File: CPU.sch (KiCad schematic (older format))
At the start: 13 parts, among them J4 SWD, U1 STM32F405RGTx, Y1 8MHz

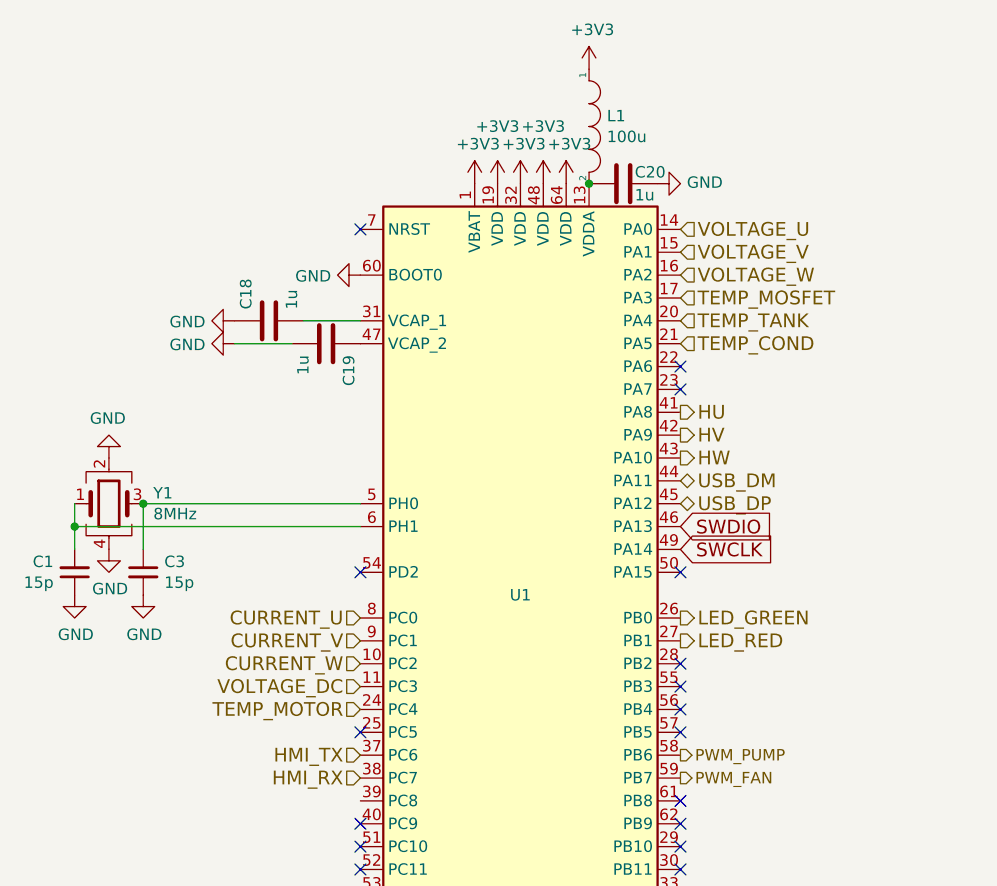
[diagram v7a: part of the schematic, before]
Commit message: - switched fan MOSFET for something beefier - switched fan diode for SMC - added BOOT0 jumper - changed fan header to 3pin - removed motor thermistor - reused condenser thermistor for return temperature sensing
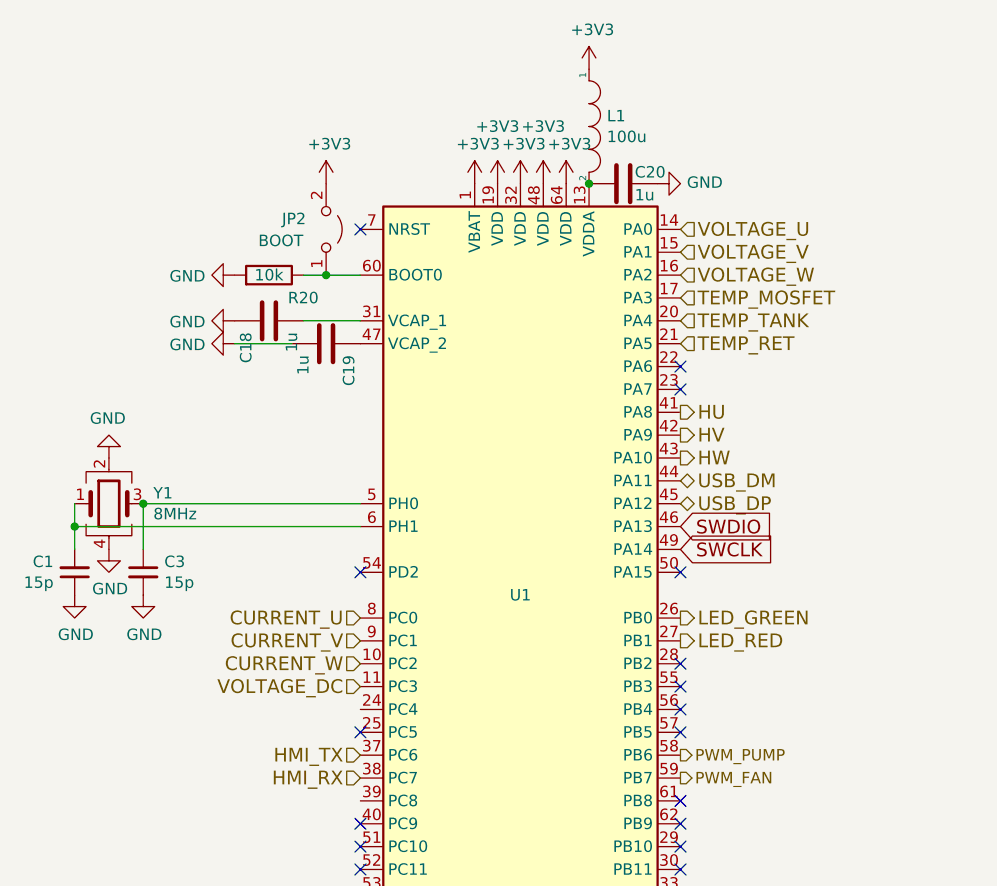
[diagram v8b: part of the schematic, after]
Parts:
- added JP2: BOOT, Jumper:SolderJumper-2_P1.3mm_Open_RoundedPad1.0x1.5mm, symbol Jumper:Jumper_2_Open
- added R20: 10k, Resistor_SMD:R_0805_2012Metric, symbol Device:R
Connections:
- net +3V3: now also JP2.2 (B)
- net GND: now also R20.2; no longer U1.60 (BOOT0)
- net TEMP_COND renamed TEMP_RET
- net TEMP_MOTOR: no longer names the net of U1.24 (PC4)
- new net: JP2.1 (A), R20.1, U1.60 (BOOT0)
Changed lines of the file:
@@
 Text HLabel 5000 4100 0    60   Input ~ 0
 HMI_RX
-Text HLabel 5000 3800 0    60   Input ~ 0
-TEMP_MOTOR
 Text HLabel 6400 4900 2    60   Output ~ 0
 LW
@@
 LU
 Text HLabel 6400 2200 2    60   Input ~ 0
-TEMP_COND
+TEMP_RET
 Text HLabel 6400 2500 2    60   Output ~ 0
 HU
@@
 $EndComp
 $Comp
-L Device:C C18
-U 1 1 53F757B5
-P 4600 2100
-AR Path="/53F757B5" Ref="C18"  Part="1"
-AR Path="/5899E230/53F757B5" Ref="C18"  Part="1"
-F 0 "C18" H 4650 2200 50  0000 L CNN
-F 1 "1u" H 4650 2000 50  0000 L CNN
-F 2 "Capacitor_SMD:C_0805_2012Metric" H 4600 2100 60  0001 C CNN
-F 3 "" H 4600 2100 60  0001 C CNN
-	1    4600 2100
-	0    -1   -1   0
-$EndComp
-$Comp
 L Device:C C19
 U 1 1 53F757AE
@@
 NoConn ~ 6400 3200
 NoConn ~ 6400 3600
-$Comp
-L power:GND #PWR0116
-U 1 1 5EE78F0F
-P 5000 1900
-F 0 "#PWR0116" H 5000 1650 50  0001 C CNN
-F 1 "GND" V 5005 1772 50  0000 R CNN
-F 2 "" H 5000 1900 50  0001 C CNN
-F 3 "" H 5000 1900 50  0001 C CNN
-	1    5000 1900
-	0    1    1    0
-$EndComp
 NoConn ~ 6400 3800
 NoConn ~ 6400 3900
@@
 NoConn ~ 6400 4400
 NoConn ~ 6400 3700
+$Comp
+L Device:C C18
+U 1 1 53F757B5
+P 4600 2100
+AR Path="/53F757B5" Ref="C18"  Part="1"
+AR Path="/5899E230/53F757B5" Ref="C18"  Part="1"
+F 0 "C18" H 4650 2200 50  0000 L CNN
+F 1 "1u" H 4650 2000 50  0000 L CNN
+F 2 "Capacitor_SMD:C_0805_2012Metric" H 4600 2100 60  0001 C CNN
+F 3 "" H 4600 2100 60  0001 C CNN
+	1    4600 2100
+	0    -1   1    0
+$EndComp
+$Comp
+L power:GND #PWR0116
+U 1 1 5EE78F0F
+P 4450 1900
+F 0 "#PWR0116" H 4450 1650 50  0001 C CNN
+F 1 "GND" V 4455 1772 50  0000 R CNN
+F 2 "" H 4450 1900 50  0001 C CNN
+F 3 "" H 4450 1900 50  0001 C CNN
+	1    4450 1900
+	0    1    1    0
+$EndComp
+$Comp
+L Device:R R20
+U 1 1 6168EF04
+P 4600 1900
+F 0 "R20" V 4500 2050 50  0000 C CNN
+F 1 "10k" V 4600 1900 50  0000 C CNN
+F 2 "Resistor_SMD:R_0805_2012Metric" V 4530 1900 50  0001 C CNN
+F 3 "~" H 4600 1900 50  0001 C CNN
+	1    4600 1900
+	0    1    -1   0
+$EndComp
+Wire Wire Line
+	4750 1900 4850 1900
+$Comp
+L Jumper:Jumper_2_Open JP2
+U 1 1 6168FCAC
+P 4850 1700
+F 0 "JP2" V 4896 1612 50  0000 R CNN
+F 1 "BOOT" V 4800 1600 50  0000 R CNN
+F 2 "Jumper:SolderJumper-2_P1.3mm_Open_RoundedPad1.0x1.5mm" H 4850 1700 50  0001 C CNN
+F 3 "~" H 4850 1700 50  0001 C CNN
+	1    4850 1700
+	0    1    -1   0
+$EndComp
+Connection ~ 4850 1900
+Wire Wire Line
+	4850 1900 5000 1900
+$Comp
+L power:+3V3 #PWR0179
+U 1 1 61690991
+P 4850 1500
+F 0 "#PWR0179" H 4850 1350 50  0001 C CNN
+F 1 "+3V3" H 4865 1673 50  0000 C CNN
+F 2 "" H 4850 1500 50  0001 C CNN
+F 3 "" H 4850 1500 50  0001 C CNN
+	1    4850 1500
+	1    0    0    -1
+$EndComp
 $EndSCHEMATC
